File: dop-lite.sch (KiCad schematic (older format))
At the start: 23 parts, among them J1 Power Input, J2 Power Output, Q1 NMOS 40V×5A Vgsth<3, Q2 IRF7319, SW1 ON/OFF button, U1 IP2721_PHY, U2 LM2574N−12G_PHY

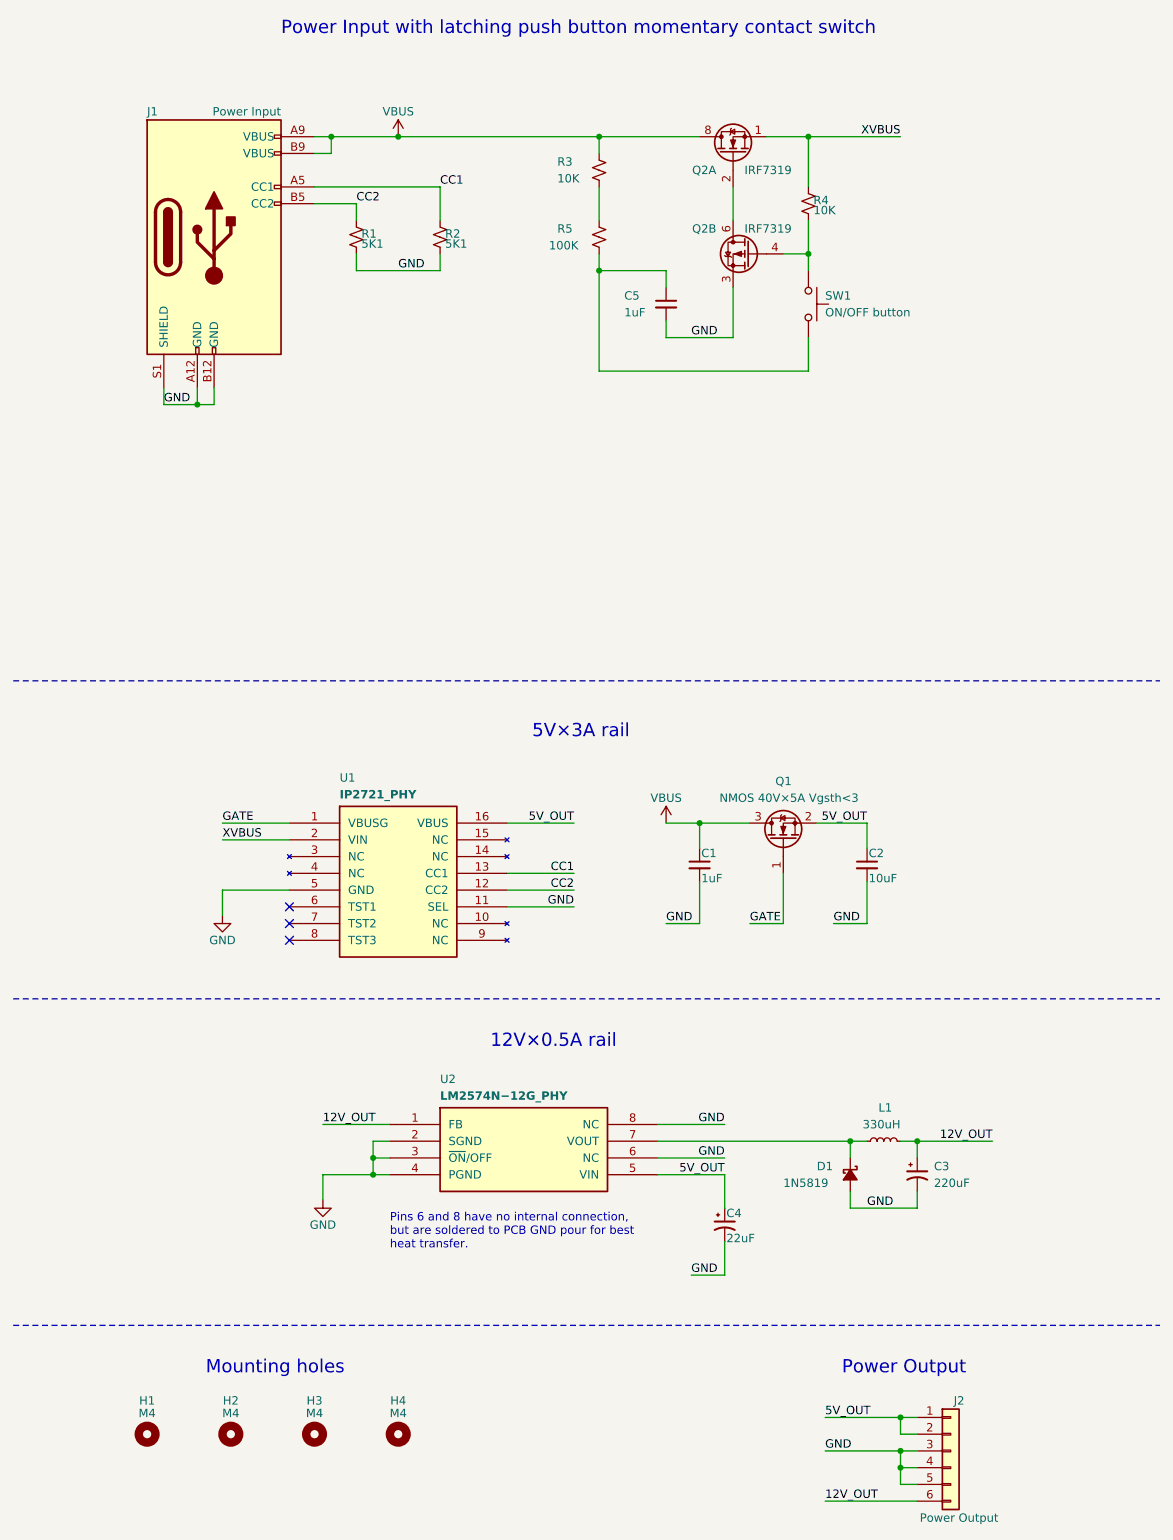
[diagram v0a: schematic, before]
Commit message: Renumbering of components
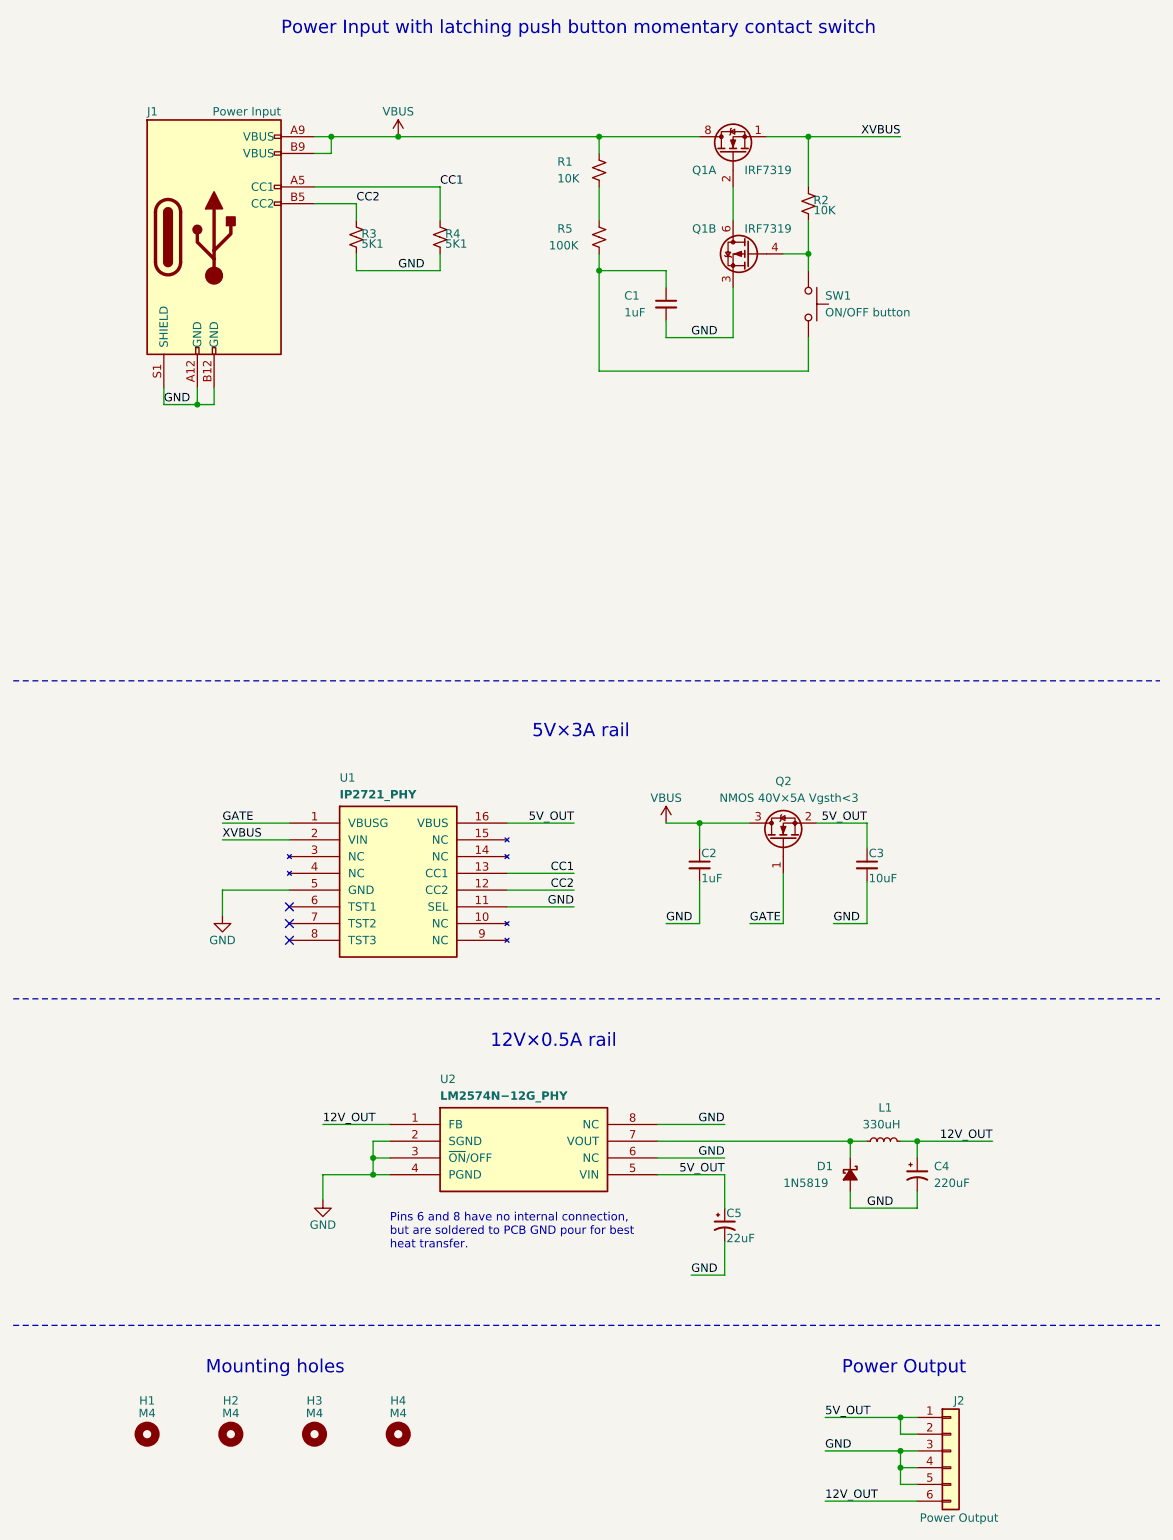
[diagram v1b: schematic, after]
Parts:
- renumbered C5 to C1, C1 to C2, C2 to C3, C3 to C4, C4 to C5, Q2 to Q1, Q1 to Q2, R3 to R1, R4 to R2, R1 to R3, R2 to R4
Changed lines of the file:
@@
 $EndComp
 $Comp
-L Device:Q_NMOS_GSD Q1
+L Device:Q_NMOS_GSD Q2
 U 1 1 62A1EC31
 P 5300 5800
-F 0 "Q1" V 5650 5750 50  0000 L CNN
+F 0 "Q2" V 5650 5750 50  0000 L CNN
 F 1 "NMOS 40V×5A Vgsth<3" V 5550 5350 50  0000 L CNN
 F 2 "Package_TO_SOT_SMD:SOT-23" H 5500 5900 50  0001 C CNN
@@
 $EndComp
 $Comp
-L Device:R_Small_US R1
+L Device:R_Small_US R3
 U 1 1 62A1FD1C
 P 2750 2200
-F 0 "R1" H 2780 2220 50  0000 L CNN
+F 0 "R3" H 2780 2220 50  0000 L CNN
 F 1 "5K1" H 2780 2160 50  0000 L CNN
 F 2 "Resistor_SMD:R_0805_2012Metric_Pad1.20x1.40mm_HandSolder" H 2750 2200 50  0001 C CNN
@@
 $EndComp
 $Comp
-L Device:R_Small_US R2
+L Device:R_Small_US R4
 U 1 1 62A23A8B
 P 3250 2200
-F 0 "R2" H 3280 2220 50  0000 L CNN
+F 0 "R4" H 3280 2220 50  0000 L CNN
 F 1 "5K1" H 3280 2160 50  0000 L CNN
 F 2 "Resistor_SMD:R_0805_2012Metric_Pad1.20x1.40mm_HandSolder" H 3250 2200 50  0001 C CNN
@@
 $EndComp
 $Comp
-L Device:C_Small C1
+L Device:C_Small C2
 U 1 1 62A24503
 P 4800 5950
-F 0 "C1" H 4810 6020 50  0000 L CNN
+F 0 "C2" H 4810 6020 50  0000 L CNN
 F 1 "1uF" H 4810 5870 50  0000 L CNN
 F 2 "Capacitor_SMD:C_0805_2012Metric_Pad1.18x1.45mm_HandSolder" H 4800 5950 50  0001 C CNN
@@
 $EndComp
 $Comp
-L Device:C_Small C2
+L Device:C_Small C3
 U 1 1 62A27C6F
 P 5800 5950
-F 0 "C2" H 5810 6020 50  0000 L CNN
+F 0 "C3" H 5810 6020 50  0000 L CNN
 F 1 "10uF" H 5810 5870 50  0000 L CNN
 F 2 "Capacitor_SMD:C_0805_2012Metric_Pad1.18x1.45mm_HandSolder" H 5800 5950 50  0001 C CNN
@@
 NoConn ~ 2350 6400
 $Comp
-L Device:CP1_Small C4
+L Device:CP1_Small C5
 U 1 1 62A2A1E6
 P 4950 8100
-F 0 "C4" H 4960 8170 50  0000 L CNN
+F 0 "C5" H 4960 8170 50  0000 L CNN
 F 1 "22uF" H 4960 8020 50  0000 L CNN
 F 2 "Capacitor_SMD:C_0805_2012Metric_Pad1.18x1.45mm_HandSolder" H 4950 8100 50  0001 C CNN
@@
 $EndComp
 $Comp
-L Device:CP1_Small C3
+L Device:CP1_Small C4
 U 1 1 62A2A5C2
 P 6100 7800
-F 0 "C3" H 6200 7850 50  0000 L CNN
+F 0 "C4" H 6200 7850 50  0000 L CNN
 F 1 "220uF" H 6200 7750 50  0000 L CNN
 F 2 "Capacitor_THT:CP_Radial_D8.0mm_P3.50mm" H 6100 7800 50  0001 C CNN
@@
 Power Output
 $Comp
-L power:GND #PWR0101
+L power:GND #PWR03
 U 1 1 62A8F091
 P 1950 6250
-F 0 "#PWR0101" H 1950 6000 50  0001 C CNN
+F 0 "#PWR03" H 1950 6000 50  0001 C CNN
 F 1 "GND" H 1950 6100 50  0000 C CNN
 F 2 "" H 1950 6250 50  0001 C CNN
@@
 	6100 8000 6100 7900
 $Comp
-L power:GND #PWR0102
+L power:GND #PWR04
 U 1 1 62A96D55
 P 2550 7950
-F 0 "#PWR0102" H 2550 7700 50  0001 C CNN
+F 0 "#PWR04" H 2550 7700 50  0001 C CNN
 F 1 "GND" H 2550 7800 50  0000 C CNN
 F 2 "" H 2550 7950 50  0001 C CNN
@@
 	2500 1600 2600 1600
 $Comp
-L power:VBUS #PWR0105
+L power:VBUS #PWR02
 U 1 1 62A9C9E9
 P 4600 5700
-F 0 "#PWR0105" H 4600 5550 50  0001 C CNN
+F 0 "#PWR02" H 4600 5550 50  0001 C CNN
 F 1 "VBUS" H 4600 5850 50  0000 C CNN
 F 2 "" H 4600 5700 50  0001 C CNN
@@
 $EndComp
 $Comp
-L power:VBUS #PWR0103
+L power:VBUS #PWR01
 U 1 1 62A987F5
 P 3000 1600
-F 0 "#PWR0103" H 3000 1450 50  0001 C CNN
+F 0 "#PWR01" H 3000 1450 50  0001 C CNN
 F 1 "VBUS" H 3000 1750 50  0000 C CNN
 F 2 "" H 3000 1600 50  0001 C CNN
@@
 	700  4850 7550 4850
 $Comp
-L Transistor_FET:IRF7343PBF Q2
+L Transistor_FET:IRF7343PBF Q1
 U 2 1 62A612E9
 P 5100 2300
-F 0 "Q2" H 5300 2450 50  0000 L CNN
+F 0 "Q1" H 5300 2450 50  0000 L CNN
 F 1 "IRF7319" H 4850 2450 50  0000 L CNN
 F 2 "Package_SO:SOIC-8_3.9x4.9mm_P1.27mm" H 5300 2225 50  0001 L CNN
@@
 $EndComp
 $Comp
-L Transistor_FET:IRF7343PBF Q2
+L Transistor_FET:IRF7343PBF Q1
 U 1 1 62A62B58
 P 5000 1700
-F 0 "Q2" V 4900 1800 50  0000 L CNN
+F 0 "Q1" V 4900 1800 50  0000 L CNN
 F 1 "IRF7319" V 4900 1350 50  0000 L CNN
 F 2 "Package_SO:SOIC-8_3.9x4.9mm_P1.27mm" H 5200 1625 50  0001 L CNN
@@
 $EndComp
 $Comp
-L Device:R_Small_US R3
+L Device:R_Small_US R1
 U 1 1 62A6BD65
 P 4200 1800
-F 0 "R3" H 3950 1850 50  0000 L CNN
+F 0 "R1" H 3950 1850 50  0000 L CNN
 F 1 "10K" H 3950 1750 50  0000 L CNN
 F 2 "Resistor_SMD:R_0805_2012Metric_Pad1.20x1.40mm_HandSolder" H 4200 1800 50  0001 C CNN
@@
 $EndComp
 $Comp
-L Device:R_Small_US R4
+L Device:R_Small_US R2
 U 1 1 62A6C8FB
 P 5450 2000
-F 0 "R4" H 5480 2020 50  0000 L CNN
+F 0 "R2" H 5480 2020 50  0000 L CNN
 F 1 "10K" H 5480 1960 50  0000 L CNN
 F 2 "Resistor_SMD:R_0805_2012Metric_Pad1.20x1.40mm_HandSolder" H 5450 2000 50  0001 C CNN
@@
 $EndComp
 $Comp
-L Device:C_Small C5
+L Device:C_Small C1
 U 1 1 62A6CC9E
 P 4600 2600
-F 0 "C5" H 4350 2650 50  0000 L CNN
+F 0 "C1" H 4350 2650 50  0000 L CNN
 F 1 "1uF" H 4350 2550 50  0000 L CNN
 F 2 "Capacitor_SMD:C_0805_2012Metric_Pad1.18x1.45mm_HandSolder" H 4600 2600 50  0001 C CNN

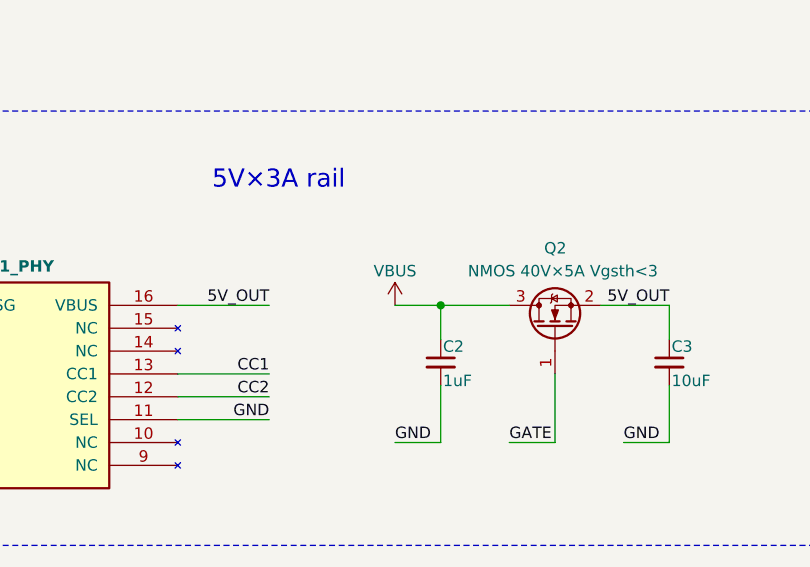
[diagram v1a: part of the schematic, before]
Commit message: fixed wrong use of vbus vs xvbus, finished pcb draft
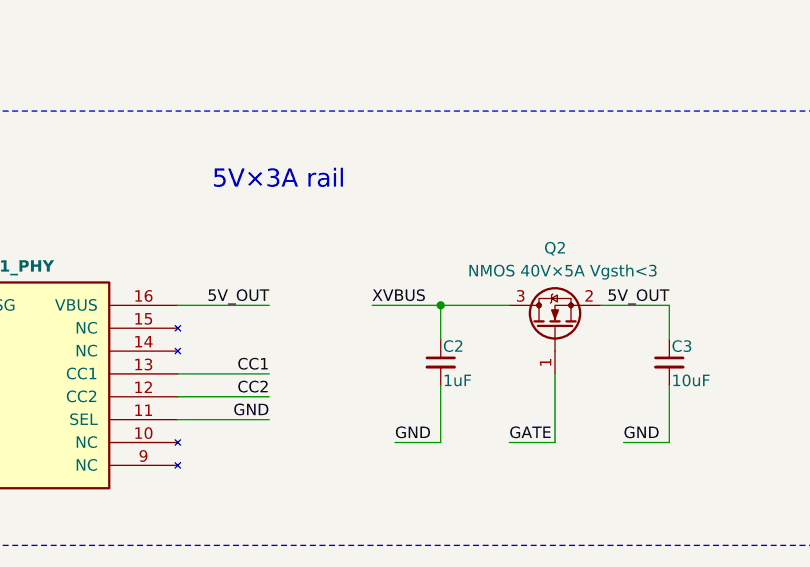
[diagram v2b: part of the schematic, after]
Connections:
- net VBUS: no longer C2.1, Q2.3 (D)
- net XVBUS: now also C2.1, Q2.3 (D)
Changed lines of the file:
@@
 Wire Wire Line
 	2500 1600 2600 1600
-$Comp
-L power:VBUS #PWR02
-U 1 1 62A9C9E9
-P 4600 5700
-F 0 "#PWR02" H 4600 5550 50  0001 C CNN
-F 1 "VBUS" H 4600 5850 50  0000 C CNN
-F 2 "" H 4600 5700 50  0001 C CNN
-F 3 "" H 4600 5700 50  0001 C CNN
-	1    4600 5700
-	1    0    0    -1
-$EndComp
-Wire Wire Line
-	4600 5700 4800 5700
 Connection ~ 4800 5700
 Text Label 5800 5700 2    50   ~ 0
@@
 Wire Wire Line
 	4200 1600 4800 1600
+Text Label 4500 5700 0    50   ~ 0
+XVBUS
+Wire Wire Line
+	4500 5700 4800 5700
 $EndSCHEMATC
